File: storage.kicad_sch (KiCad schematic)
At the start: 39 parts, among them J6 Micro_SD_Card_Det1, U1 MIMX8MM6DVTLZAA, U24 TPD4E02B04, U25 W25Q32JWZP, U26 TPD4E02B04, U27 D5V0H1B2LP, U28 SiP32431DR3, U29 EMMC, U30 74LVC2G07

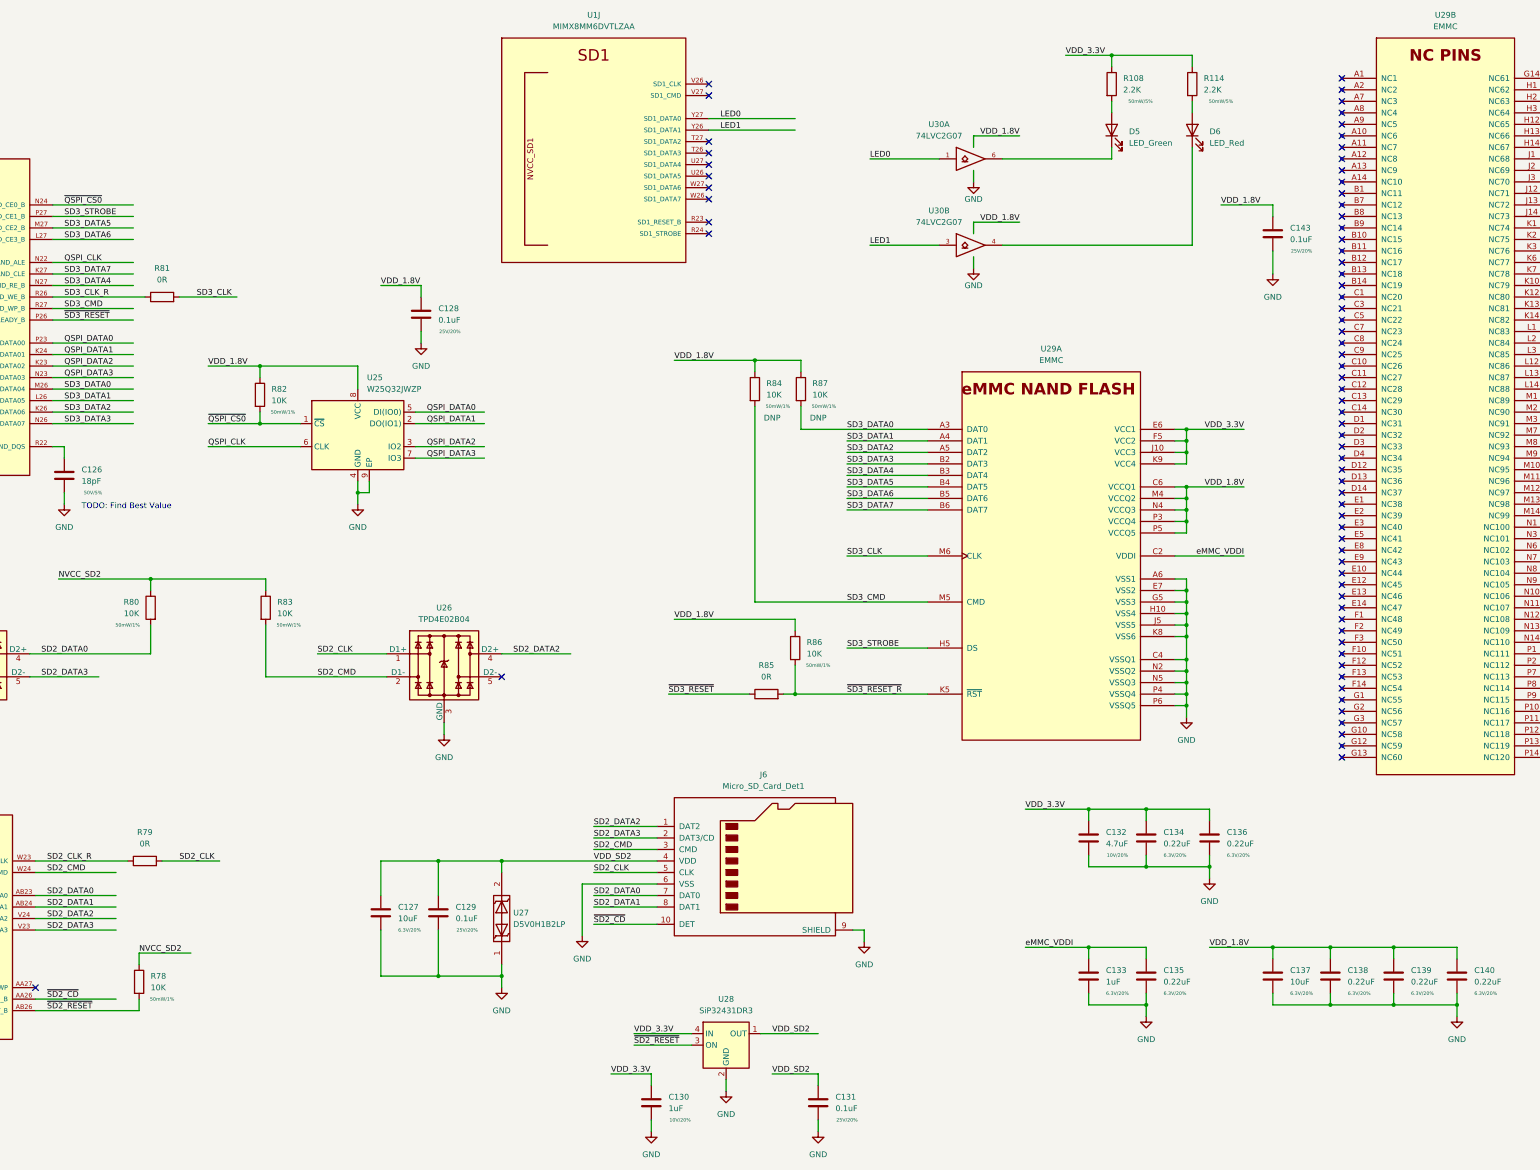
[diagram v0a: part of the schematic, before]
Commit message: ddr length matching work, misc cleanup
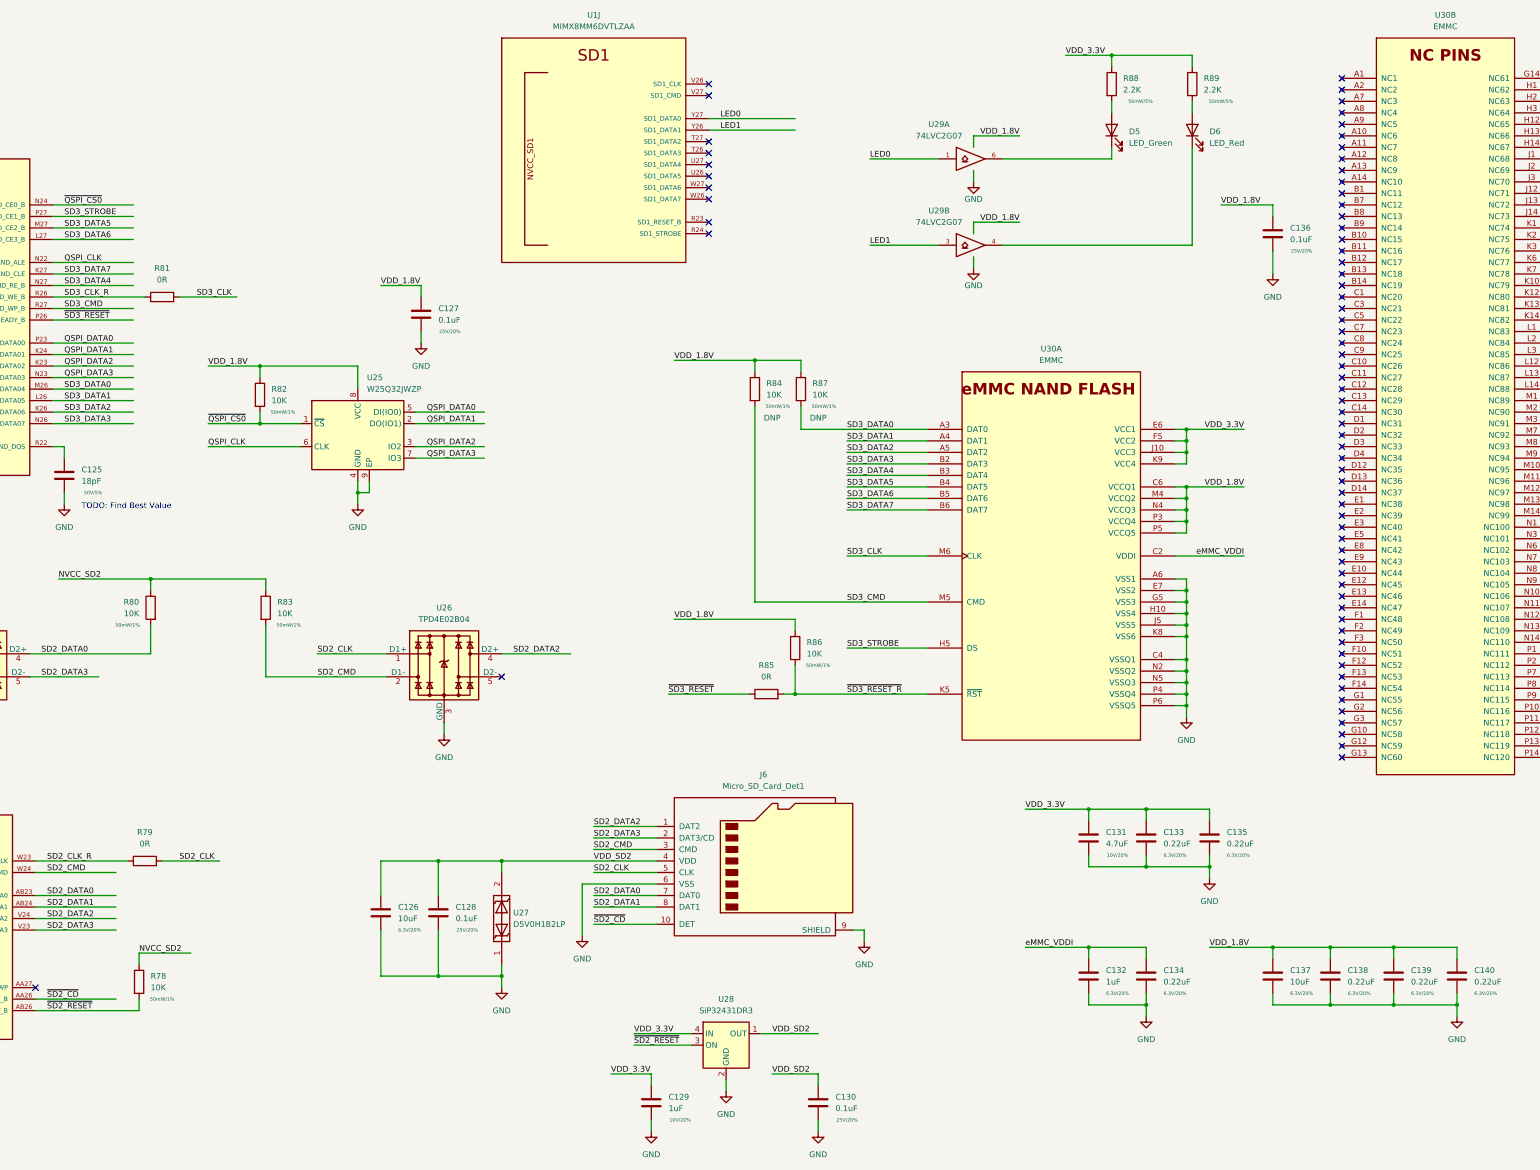
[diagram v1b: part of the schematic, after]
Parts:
- renumbered C126 to C125, C127 to C126, C128 to C127, C129 to C128, C130 to C129, C131 to C130, C132 to C131, C133 to C132, C134 to C133, C135 to C134, C136 to C135, C143 to C136, R108 to R88, R114 to R89, U30 to U29, U29 to U30
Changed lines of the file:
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@@
   (symbol (lib_id "Device:C") (at 300.99 228.6 0) (unit 1)
     (in_bom yes) (on_board yes)
-    (property "Reference" "C133" (id 0) (at 304.8 227.3299 0)
+    (property "Reference" "C132" (id 0) (at 304.8 227.3299 0)
       (effects (font (size 1.27 1.27)) (justify left))
     )
@@
   (symbol (lib_id "Device:C") (at 144.78 214.63 0) (unit 1)
     (in_bom yes) (on_board yes)
-    (property "Reference" "C127" (id 0) (at 148.59 213.3599 0)
+    (property "Reference" "C126" (id 0) (at 148.59 213.3599 0)
       (effects (font (size 1.27 1.27)) (justify left))
     )
@@
   (symbol (lib_id "Device:C") (at 300.99 198.12 0) (unit 1)
     (in_bom yes) (on_board yes)
-    (property "Reference" "C132" (id 0) (at 304.8 196.8499 0)
+    (property "Reference" "C131" (id 0) (at 304.8 196.8499 0)
       (effects (font (size 1.27 1.27)) (justify left))
     )
@@
   (symbol (lib_id "Device:R") (at 323.85 31.75 0) (unit 1)
     (in_bom yes) (on_board yes)
-    (property "Reference" "R114" (id 0) (at 326.39 30.4799 0)
+    (property "Reference" "R89" (id 0) (at 326.39 30.4799 0)
       (effects (font (size 1.27 1.27)) (justify left))
     )
@@
   (symbol (lib_id "power:GND") (at 313.69 237.49 0) (unit 1)
     (in_bom yes) (on_board yes) (fields_autoplaced)
-    (property "Reference" "#PWR0127" (id 0) (at 313.69 243.84 0)
+    (property "Reference" "#PWR0129" (id 0) (at 313.69 243.84 0)
       (effects (font (size 1.27 1.27)) hide)
     )
@@
   (symbol (lib_id "Device:C") (at 313.69 228.6 0) (unit 1)
     (in_bom yes) (on_board yes)
-    (property "Reference" "C135" (id 0) (at 317.5 227.3299 0)
+    (property "Reference" "C134" (id 0) (at 317.5 227.3299 0)
       (effects (font (size 1.27 1.27)) (justify left))
     )
@@
   (symbol (lib_id "Device:C") (at 204.47 256.54 0) (unit 1)
     (in_bom yes) (on_board yes)
-    (property "Reference" "C130" (id 0) (at 208.28 255.2699 0)
+    (property "Reference" "C129" (id 0) (at 208.28 255.2699 0)
       (effects (font (size 1.27 1.27)) (justify left))
     )
@@
   (symbol (lib_id "power:GND") (at 382.27 237.49 0) (unit 1)
     (in_bom yes) (on_board yes) (fields_autoplaced)
-    (property "Reference" "#PWR0130" (id 0) (at 382.27 243.84 0)
+    (property "Reference" "#PWR0133" (id 0) (at 382.27 243.84 0)
       (effects (font (size 1.27 1.27)) hide)
     )
@@
   (symbol (lib_id "power:GND") (at 341.63 73.66 0) (unit 1)
     (in_bom yes) (on_board yes) (fields_autoplaced)
-    (property "Reference" "#PWR0140" (id 0) (at 341.63 80.01 0)
+    (property "Reference" "#PWR0132" (id 0) (at 341.63 80.01 0)
       (effects (font (size 1.27 1.27)) hide)
     )
@@
   (symbol (lib_id "power:GND") (at 322.58 171.45 0) (unit 1)
     (in_bom yes) (on_board yes) (fields_autoplaced)
-    (property "Reference" "#PWR0128" (id 0) (at 322.58 177.8 0)
+    (property "Reference" "#PWR0130" (id 0) (at 322.58 177.8 0)
       (effects (font (size 1.27 1.27)) hide)
     )
@@
   (symbol (lib_id "Device:C") (at 327.66 198.12 0) (unit 1)
     (in_bom yes) (on_board yes)
-    (property "Reference" "C136" (id 0) (at 331.47 196.8499 0)
+    (property "Reference" "C135" (id 0) (at 331.47 196.8499 0)
       (effects (font (size 1.27 1.27)) (justify left))
     )
@@
   (symbol (lib_id "qsbc:EMMC") (at 292.1 95.25 0) (unit 1)
     (in_bom yes) (on_board yes) (fields_autoplaced)
-    (property "Reference" "U29" (id 0) (at 292.735 90.17 0))
+    (property "Reference" "U30" (id 0) (at 292.735 90.17 0))
     (property "Value" "EMMC" (id 1) (at 292.735 92.71 0))
     (property "Footprint" "qsbc:FBGA-153" (id 2) (at 292.1 95.25 0)
@@
   (symbol (lib_id "Device:C") (at 157.48 214.63 0) (unit 1)
     (in_bom yes) (on_board yes)
-    (property "Reference" "C129" (id 0) (at 161.29 213.3599 0)
+    (property "Reference" "C128" (id 0) (at 161.29 213.3599 0)
       (effects (font (size 1.27 1.27)) (justify left))
     )
@@
   (symbol (lib_id "Device:C") (at 153.67 82.55 0) (unit 1)
     (in_bom yes) (on_board yes)
-    (property "Reference" "C128" (id 0) (at 157.48 81.2799 0)
+    (property "Reference" "C127" (id 0) (at 157.48 81.2799 0)
       (effects (font (size 1.27 1.27)) (justify left))
     )
@@
   (symbol (lib_id "power:GND") (at 275.59 53.34 0) (unit 1)
     (in_bom yes) (on_board yes)
-    (property "Reference" "#PWR0134" (id 0) (at 275.59 59.69 0)
+    (property "Reference" "#PWR0127" (id 0) (at 275.59 59.69 0)
       (effects (font (size 1.27 1.27)) hide)
     )
@@
   (symbol (lib_id "power:GND") (at 275.59 72.39 0) (unit 1)
     (in_bom yes) (on_board yes)
-    (property "Reference" "#PWR0135" (id 0) (at 275.59 78.74 0)
+    (property "Reference" "#PWR0128" (id 0) (at 275.59 78.74 0)
       (effects (font (size 1.27 1.27)) hide)
     )
@@
   (symbol (lib_id "74xGxx:74LVC2G07") (at 275.59 48.26 0) (unit 1)
     (in_bom yes) (on_board yes)
-    (property "Reference" "U30" (id 0) (at 267.97 40.64 0))
+    (property "Reference" "U29" (id 0) (at 267.97 40.64 0))
     (property "Value" "74LVC2G07" (id 1) (at 267.97 43.18 0))
     (property "Footprint" "Package_TO_SOT_SMD:SOT-886" (id 2) (at 275.59 48.26 0)
@@
   (symbol (lib_id "Device:C") (at 313.69 198.12 0) (unit 1)
     (in_bom yes) (on_board yes)
-    (property "Reference" "C134" (id 0) (at 317.5 196.8499 0)
+    (property "Reference" "C133" (id 0) (at 317.5 196.8499 0)
       (effects (font (size 1.27 1.27)) (justify left))
     )
@@
   (symbol (lib_id "power:GND") (at 327.66 207.01 0) (unit 1)
     (in_bom yes) (on_board yes) (fields_autoplaced)
-    (property "Reference" "#PWR0129" (id 0) (at 327.66 213.36 0)
+    (property "Reference" "#PWR0131" (id 0) (at 327.66 213.36 0)
       (effects (font (size 1.27 1.27)) hide)
     )
@@
   (symbol (lib_id "Device:R") (at 306.07 31.75 0) (unit 1)
     (in_bom yes) (on_board yes)
-    (property "Reference" "R108" (id 0) (at 308.61 30.4799 0)
+    (property "Reference" "R88" (id 0) (at 308.61 30.4799 0)
       (effects (font (size 1.27 1.27)) (justify left))
     )
@@
   (symbol (lib_id "74xGxx:74LVC2G07") (at 275.59 67.31 0) (unit 2)
     (in_bom yes) (on_board yes)
-    (property "Reference" "U30" (id 0) (at 267.97 59.69 0))
+    (property "Reference" "U29" (id 0) (at 267.97 59.69 0))
     (property "Value" "74LVC2G07" (id 1) (at 267.97 62.23 0))
     (property "Footprint" "Package_TO_SOT_SMD:SOT-886" (id 2) (at 275.59 67.31 0)
@@
   (symbol (lib_id "Device:C") (at 74.93 118.11 0) (unit 1)
     (in_bom yes) (on_board yes)
-    (property "Reference" "C126" (id 0) (at 78.74 116.8399 0)
+    (property "Reference" "C125" (id 0) (at 78.74 116.8399 0)
       (effects (font (size 1.27 1.27)) (justify left))
     )
@@
   (symbol (lib_id "Device:C") (at 341.63 64.77 0) (unit 1)
     (in_bom yes) (on_board yes)
-    (property "Reference" "C143" (id 0) (at 345.44 63.4999 0)
+    (property "Reference" "C136" (id 0) (at 345.44 63.4999 0)
       (effects (font (size 1.27 1.27)) (justify left))
     )
@@
   (symbol (lib_id "Device:C") (at 241.3 256.54 0) (unit 1)
     (in_bom yes) (on_board yes)
-    (property "Reference" "C131" (id 0) (at 245.11 255.2699 0)
+    (property "Reference" "C130" (id 0) (at 245.11 255.2699 0)
       (effects (font (size 1.27 1.27)) (justify left))
     )
@@
   (symbol (lib_name "EMMC_1") (lib_id "qsbc:EMMC") (at 379.73 21.59 0) (unit 2)
     (in_bom yes) (on_board yes) (fields_autoplaced)
-    (property "Reference" "U29" (id 0) (at 379.73 16.51 0))
+    (property "Reference" "U30" (id 0) (at 379.73 16.51 0))
     (property "Value" "EMMC" (id 1) (at 379.73 19.05 0))
     (property "Footprint" "qsbc:FBGA-153" (id 2) (at 379.73 21.59 0)

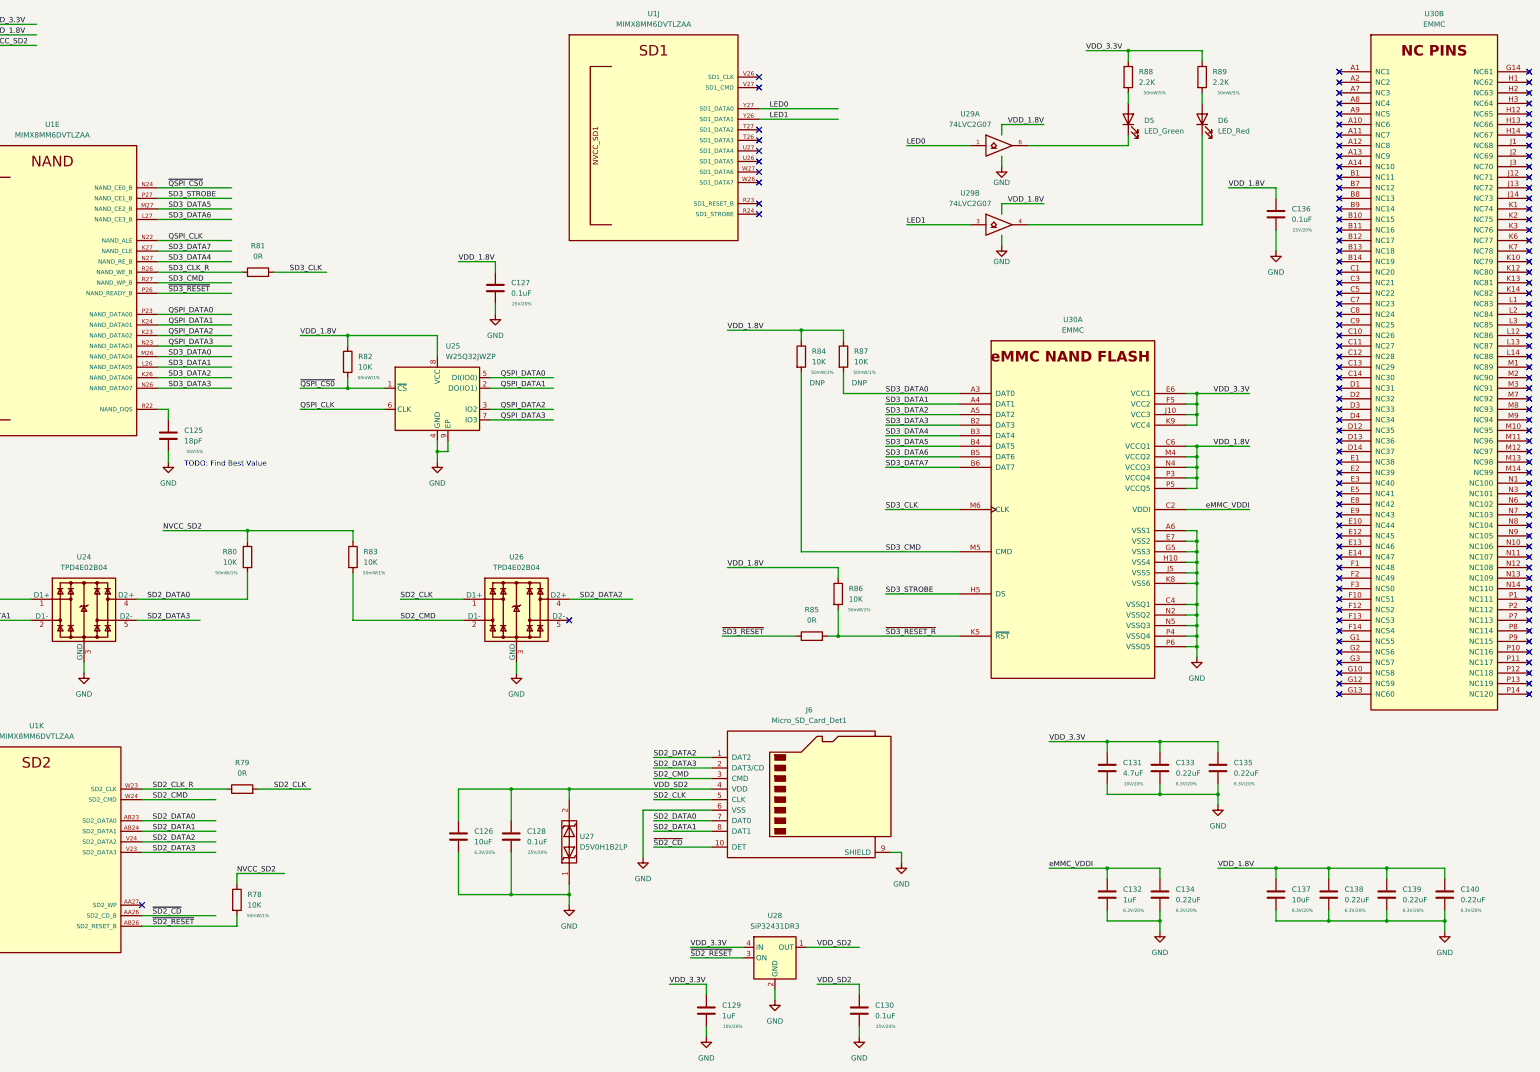
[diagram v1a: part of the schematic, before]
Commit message: misc cleanup, change from usb mux to dual uart
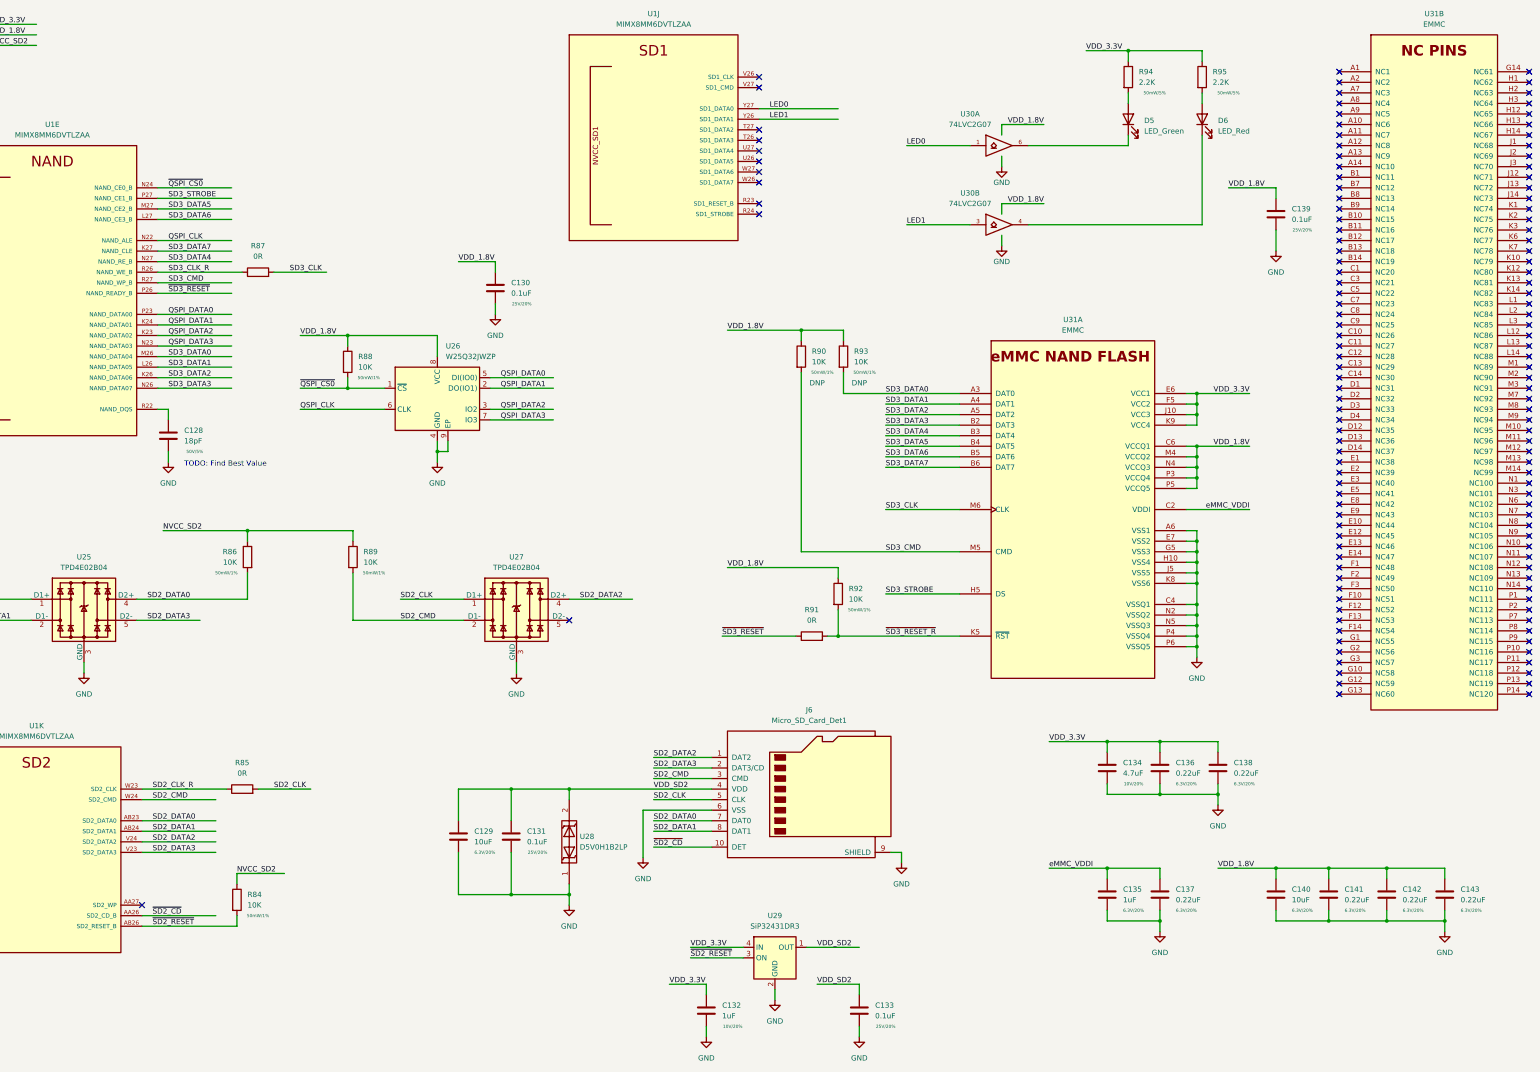
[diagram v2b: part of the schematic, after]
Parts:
- R85: renamed from R79; MPN RC0201JR-070RL -> RC0201FR-070RL
- R87: renamed from R81; MPN RC0201JR-070RL -> RC0201FR-070RL
- R91: renamed from R85; MPN RC0201JR-070RL -> RC0201FR-070RL
- renumbered C125 to C128, C126 to C129, C127 to C130, C128 to C131, C129 to C132, C130 to C133, C131 to C134, C132 to C135, C133 to C136, C134 to C137, C135 to C138, C136 to C139, C137 to C140, C138 to C141, C139 to C142, C140 to C143, R78 to R84, R80 to R86, R82 to R88, R83 to R89, R84 to R90, R86 to R92, R87 to R93, R88 to R94, R89 to R95, U24 to U25, U25 to U26, U26 to U27, U27 to U28, U28 to U29, U29 to U30, U30 to U31

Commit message: Rev 1
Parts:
- renumbered R84 to R83, R85 to R84, R86 to R85, R87 to R86, R88 to R87, R89 to R88, R90 to R89, R91 to R90, R92 to R91, R93 to R92, R94 to R93, R95 to R94
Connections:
- net GND: now also U28.2; no longer U28.1
- net VDD_SD2: now also U28.1; no longer U28.2
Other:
- moved on the sheet: U28
